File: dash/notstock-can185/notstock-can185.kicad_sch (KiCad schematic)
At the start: 31 parts, among them J1 OBD 12V GND H L K, J2 UART wires from display, J3 BAT to display, U1 LMR16006YDDCR, U2 SN65HVD230

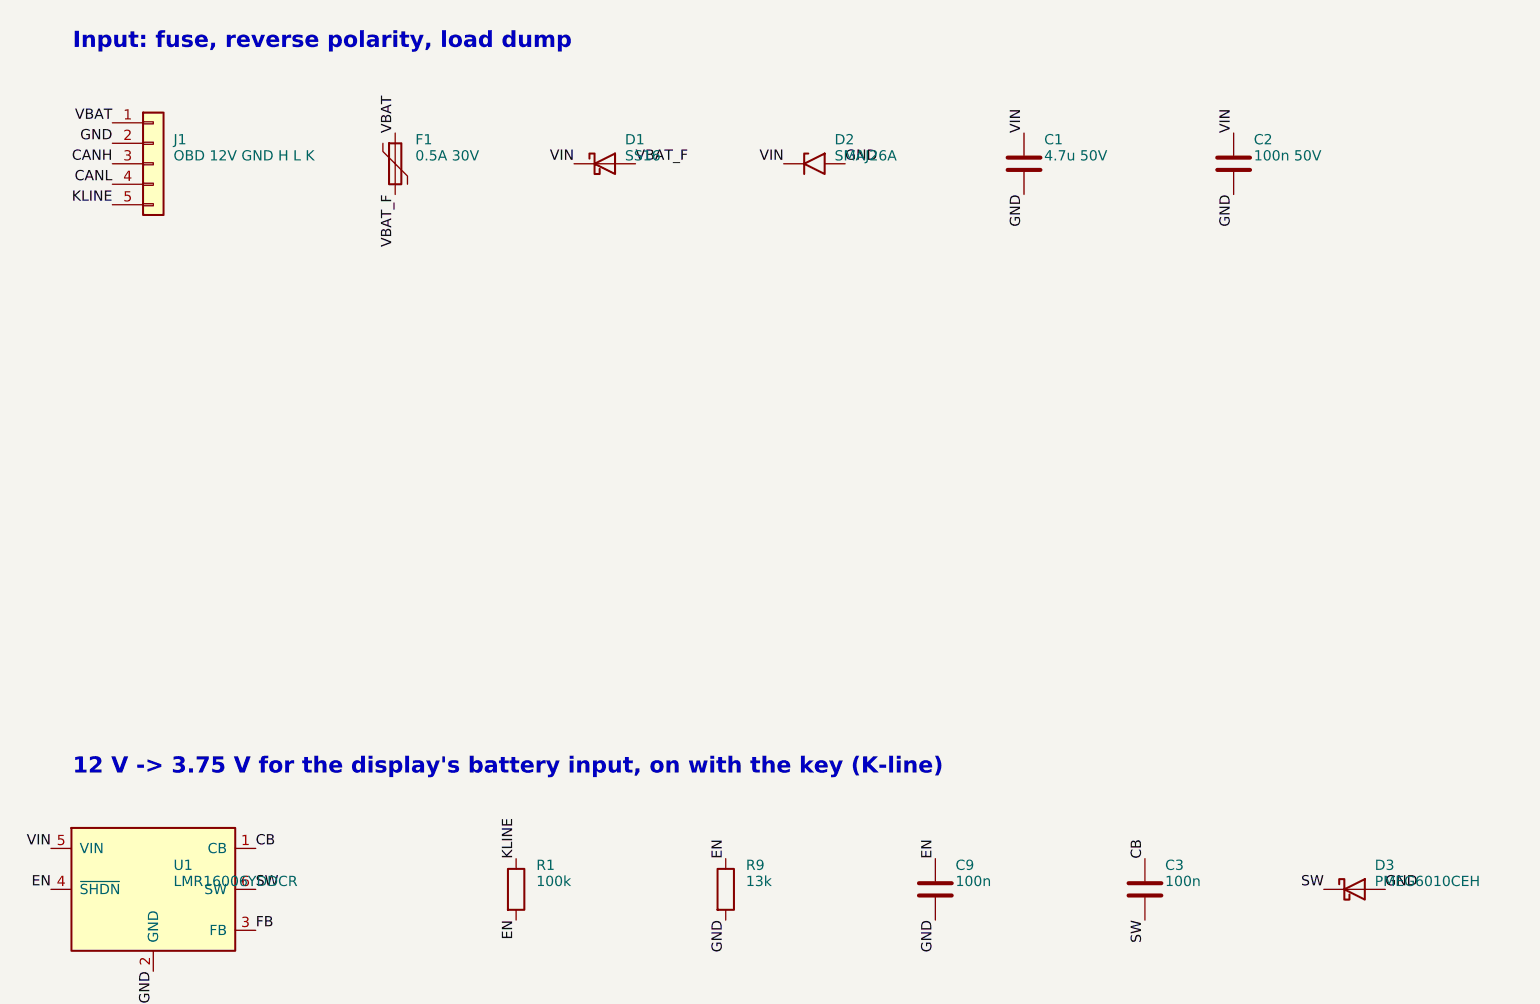
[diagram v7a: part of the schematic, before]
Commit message: CAN 1.85 rev 5: ignition from OBD pin 1 (terminal 15) instead of the K-line
VW puts terminal 15 on OBD pin 1, as the CANcheck display uses it. Same
divider onto EN; J1 pin 5 marked 15.

Co-Authored-By: Claude Opus 5.5 <noreply@anthropic.com>
Claude-Session: https://claude.ai/code/session_018SKN4tJhAPpVCWtvRZgZpD
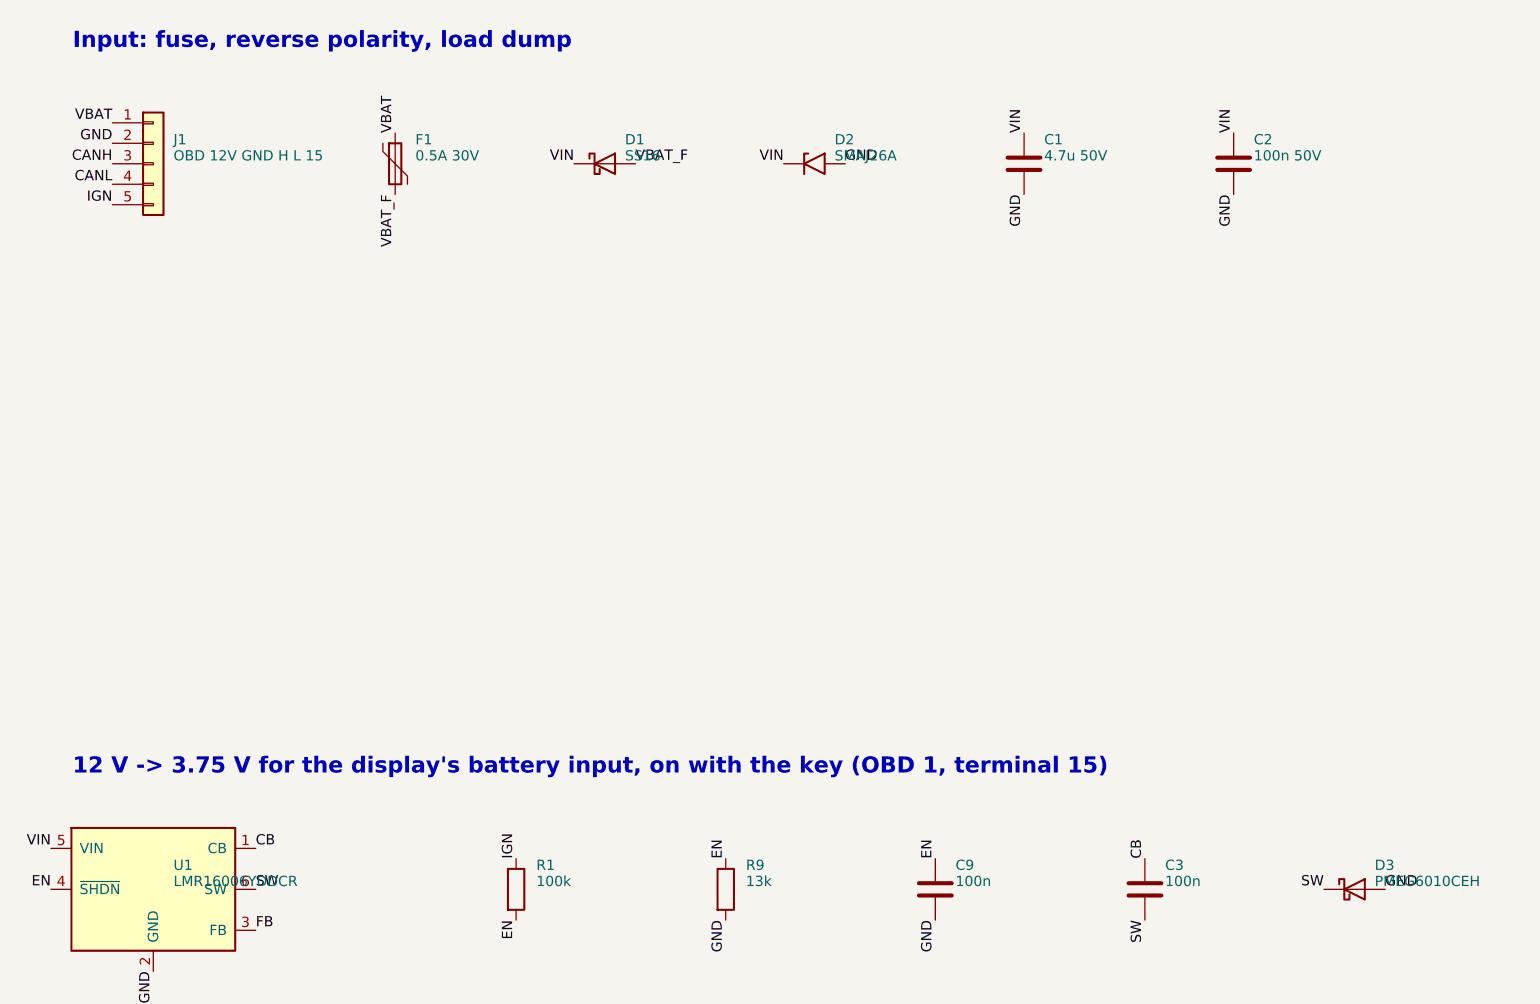
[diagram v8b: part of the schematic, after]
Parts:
- J1: value OBD 12V GND H L K -> OBD 12V GND H L 15
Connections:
- net KLINE renamed IGN
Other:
- note added: "12 V -> 3.75 V for the display's battery input, on with the key (OBD 1, terminal 15)"
- note removed: "12 V -> 3.75 V for the display's battery input, on with the key (K-line)"
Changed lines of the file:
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@@
     (property "Reference" "J1" (at 32.5 47 0)
       (effects (font (size 1.27 1.27)) (justify left)))
-    (property "Value" "OBD 12V GND H L K" (at 32.5 49 0)
+    (property "Value" "OBD 12V GND H L 15" (at 32.5 49 0)
       (effects (font (size 1.27 1.27)) (justify left)))
     (property "Footprint" "Connector_JST:JST_PH_B5B-PH-SM4-TB_1x05-1MP_P2.00mm_Vertical" (at 30 50 0)
@@
     (effects (font (size 1.27 1.27)) (justify right bottom))
   )
-  (label "KLINE" (at 24.92 55.08 180) (fields_autoplaced)
+  (label "IGN" (at 24.92 55.08 180) (fields_autoplaced)
     (effects (font (size 1.27 1.27)) (justify right bottom))
   )
@@
     (effects (font (size 1.27 1.27)) (justify right bottom))
   )
-  (text "12 V -> 3.75 V for the display's battery input, on with the key (K-line)" (at 20 126 0)
+  (text "12 V -> 3.75 V for the display's battery input, on with the key (OBD 1, terminal 15)" (at 20 126 0)
     (effects (font (size 2 2) bold) (justify left bottom))
   )
@@
     )
   )
-  (label "KLINE" (at 75 136.19 90) (fields_autoplaced)
-    (effects (font (size 1.27 1.27)) (justify left bottom))
-  )
+  (label "IGN" (at 75 136.19 90) (fields_autoplaced)
+    (effects (font (size 1.27 1.27)) (justify left bottom))
+  )
